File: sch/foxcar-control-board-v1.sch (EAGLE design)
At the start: 118 parts, among them J1 USB_MICROB, J2 MICROSD, J3 XBEE-PRO, U1 SPX29300, U2 HMC5883LSMD, U3 STM32F4V, U4 VNH5019, U6 MPU6000

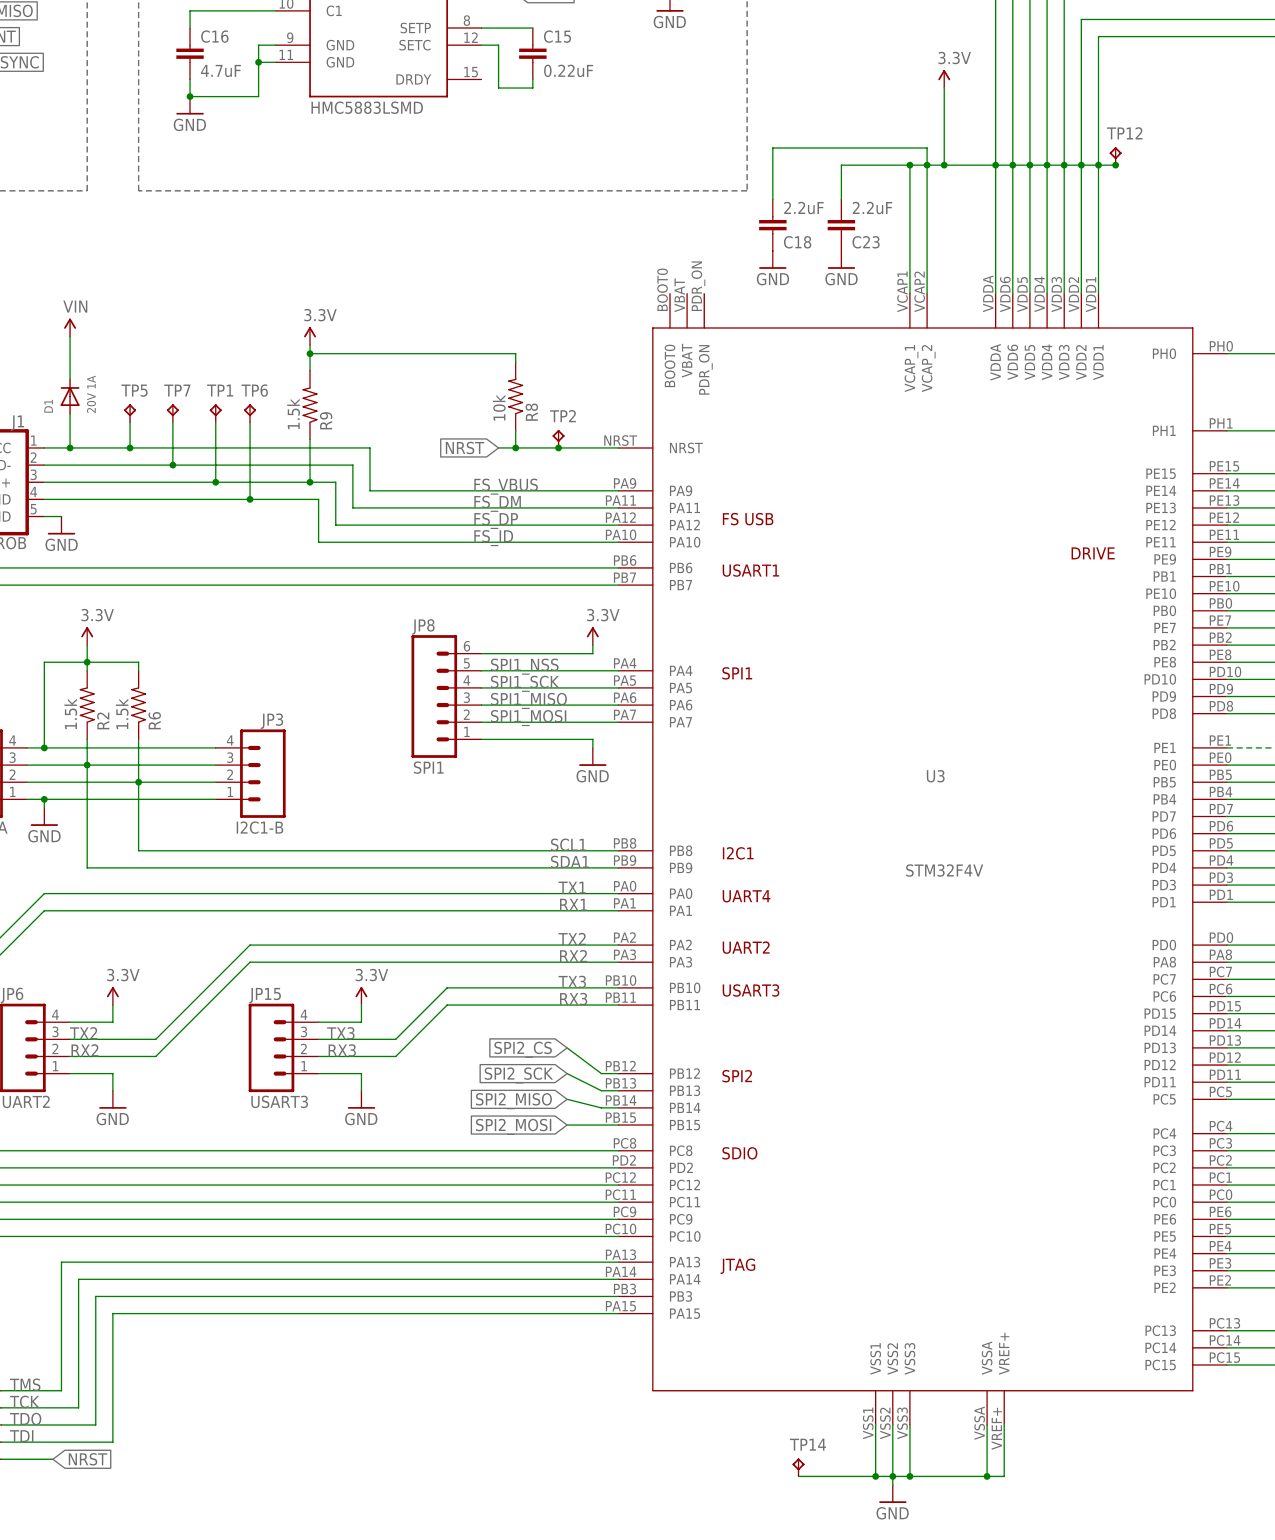
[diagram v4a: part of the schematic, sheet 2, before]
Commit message: Trying a new technique: placing all components around the stm32f4 with relatively direct paths, then seeing how badly I can fuck it up.
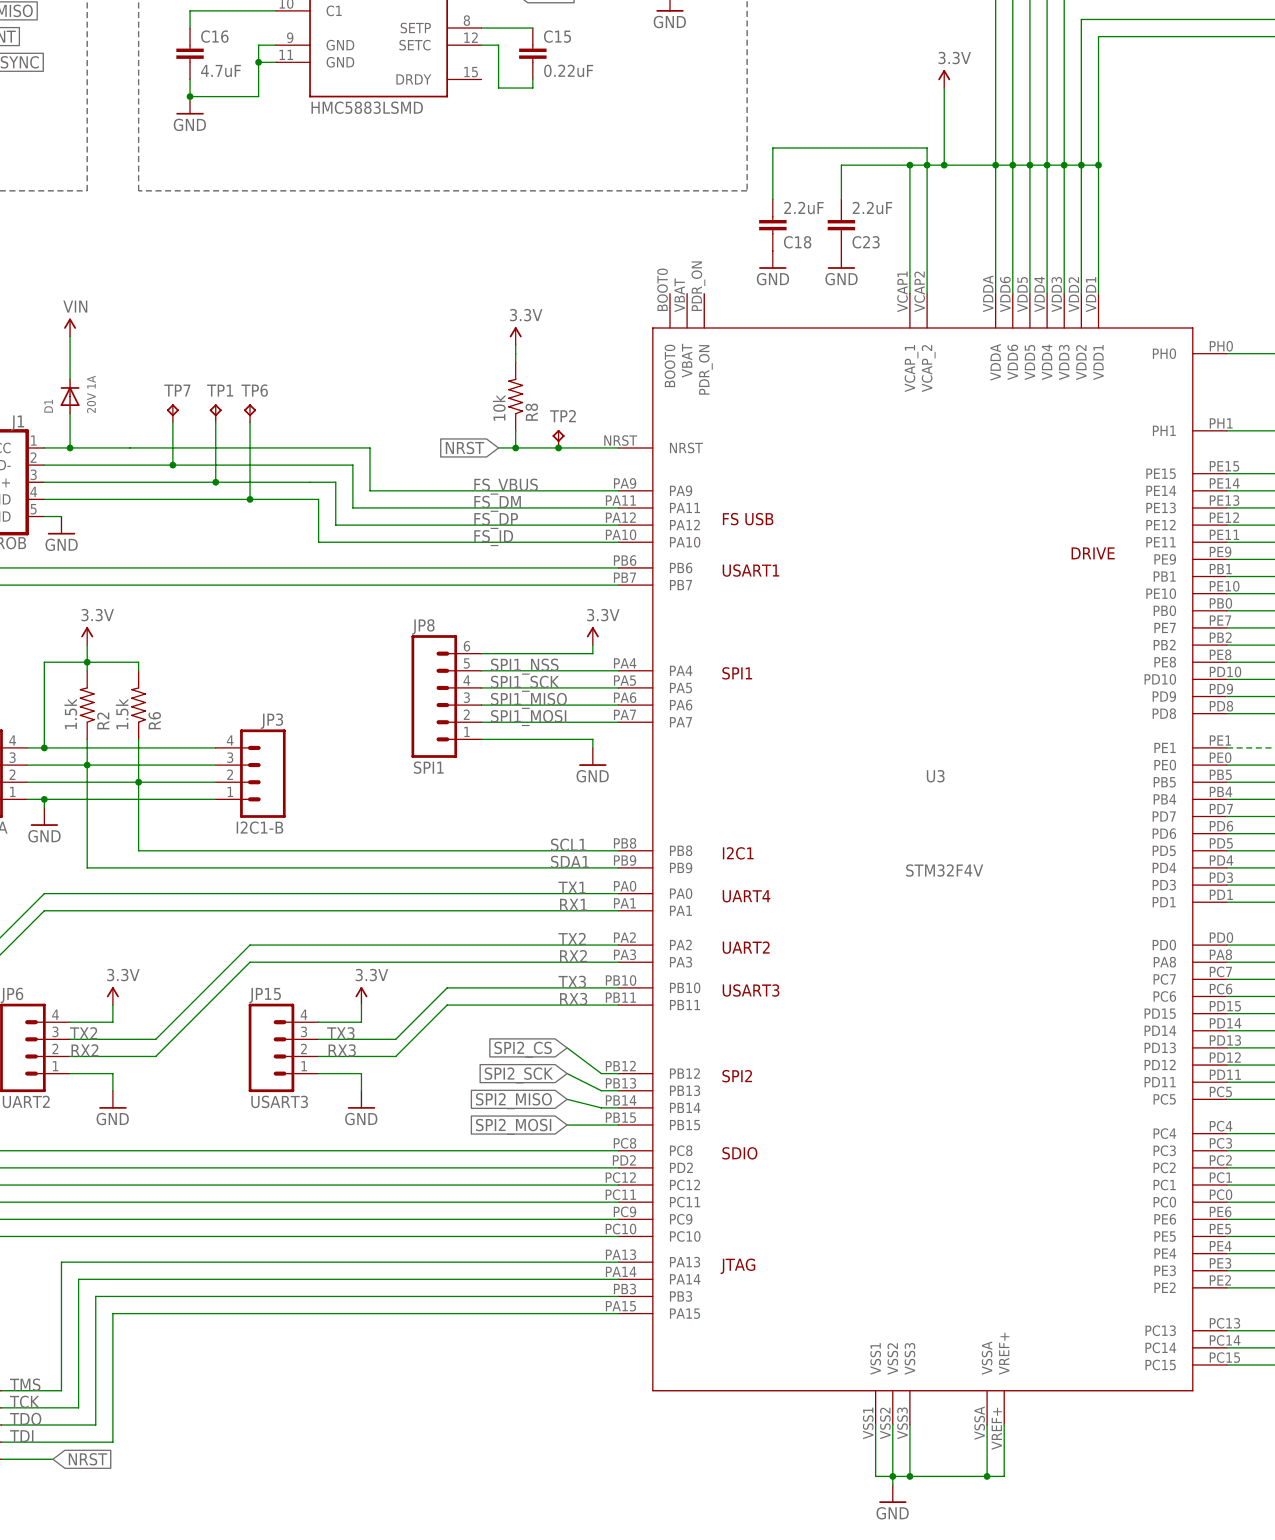
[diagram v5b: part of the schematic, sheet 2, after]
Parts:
- removed R9: 1.5k, SparkFun-Passives:RESISTOR0402-RES
- removed TP12, TP14, TP5: TPTP06R, testpad:TPTP06R
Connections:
- net 3.3V: no longer R9.2, TP12.TP
- net FS_DP: no longer R9.1
- net FS_VBUS: no longer TP5.TP
- net GND: no longer TP14.TP
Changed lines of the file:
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@@
 <part name="J1" library="SparkFun" deviceset="USB_MICROB_PLUG" device="-PTH" value="USB_MICROB"/>
 <part name="DIG_GND11" library="SparkFun-Aesthetics" deviceset="GND" device="" value="GND"/>
-<part name="R9" library="SparkFun-Passives" deviceset="RESISTOR" device="0402-RES" value="1.5k"/>
 <part name="TP1" library="testpad" deviceset="TP" device="TP06R"/>
-<part name="TP5" library="testpad" deviceset="TP" device="TP06R"/>
 <part name="TP7" library="testpad" deviceset="TP" device="TP06R"/>
 <part name="P+19" library="SparkFun-Aesthetics" deviceset="3.3V" device=""/>
@@
 <part name="DIG_GND26" library="SparkFun-Aesthetics" deviceset="GND" device="" value="GND"/>
 <part name="DIG_GND27" library="SparkFun-Aesthetics" deviceset="GND" device="" value="GND"/>
-<part name="TP12" library="testpad" deviceset="TP" device="TP06R"/>
 <part name="P+1" library="SparkFun-Aesthetics" deviceset="3.3V" device=""/>
 <part name="C21" library="SparkFun-Passives" deviceset="CAP" device="0402-CAP" value="100nF"/>
@@
 <part name="DIG_GND31" library="SparkFun-Aesthetics" deviceset="GND" device="" value="GND"/>
 <part name="DIG_GND32" library="SparkFun-Aesthetics" deviceset="GND" device="" value="GND"/>
-<part name="TP14" library="testpad" deviceset="TP" device="TP06R"/>
 <part name="C9" library="SparkFun-Passives" deviceset="CAP" device="0402-CAP" value="100nF"/>
 <part name="DIG_GND33" library="SparkFun-Aesthetics" deviceset="GND" device="" value="GND"/>
@@
 <instance part="J1" gate="G$1" x="106.68" y="165.1" rot="MR0"/>
 <instance part="DIG_GND11" gate="1" x="116.84" y="157.48" rot="MR0"/>
-<instance part="R9" gate="G$1" x="153.67" y="176.53" rot="MR90"/>
 <instance part="TP1" gate="G$1" x="139.7" y="176.53"/>
-<instance part="TP5" gate="G$1" x="127" y="176.53"/>
 <instance part="TP7" gate="G$1" x="133.35" y="176.53"/>
-<instance part="P+19" gate="G$1" x="153.67" y="185.42"/>
+<instance part="P+19" gate="G$1" x="184.15" y="185.42"/>
 <instance part="TP6" gate="G$1" x="144.78" y="176.53"/>
 <instance part="R8" gate="G$1" x="184.15" y="177.8" rot="MR90"/>
@@
 <instance part="DIG_GND26" gate="1" x="232.41" y="196.85" rot="MR0"/>
 <instance part="DIG_GND27" gate="1" x="222.25" y="196.85" rot="MR0"/>
-<instance part="TP12" gate="G$1" x="273.05" y="214.63"/>
 <instance part="P+1" gate="G$1" x="247.65" y="223.52"/>
 <instance part="C21" gate="G$1" x="356.87" y="215.9" rot="MR180"/>
@@
 <instance part="DIG_GND31" gate="1" x="330.2" y="171.45"/>
 <instance part="DIG_GND32" gate="1" x="240.03" y="13.97"/>
-<instance part="TP14" gate="G$1" x="226.06" y="20.32"/>
 <instance part="C9" gate="G$1" x="369.57" y="215.9" rot="MR180"/>
 <instance part="DIG_GND33" gate="1" x="369.57" y="205.74" rot="MR0"/>
@@
 </segment>
 <segment>
-<pinref part="R9" gate="G$1" pin="2"/>
 <pinref part="P+19" gate="G$1" pin="3.3V"/>
-<wire x1="153.67" y1="181.61" x2="153.67" y2="184.15" width="0.15" layer="91"/>
 <pinref part="R8" gate="G$1" pin="2"/>
-<wire x1="153.67" y1="184.15" x2="153.67" y2="185.42" width="0.15" layer="91"/>
 <wire x1="184.15" y1="182.88" x2="184.15" y2="184.15" width="0.15" layer="91"/>
-<wire x1="153.67" y1="184.15" x2="184.15" y2="184.15" width="0.15" layer="91"/>
-<junction x="153.67" y="184.15"/>
+<wire x1="184.15" y1="185.42" x2="184.15" y2="184.15" width="0.15" layer="91"/>
 </segment>
 <segment>
@@
 <wire x1="242.57" y1="193.04" x2="242.57" y2="212.09" width="0.15" layer="91"/>
 <pinref part="U3" gate="G$1" pin="VCAP_1"/>
-<pinref part="TP12" gate="G$1" pin="TP"/>
-<junction x="273.05" y="212.09"/>
-<wire x1="270.51" y1="212.09" x2="273.05" y2="212.09" width="0.15" layer="91"/>
 <pinref part="U3" gate="G$1" pin="VDDA"/>
 <wire x1="255.27" y1="193.04" x2="255.27" y2="212.09" width="0.15" layer="91"/>
@@
 <pinref part="DIG_GND32" gate="1" pin="GND"/>
 <junction x="240.03" y="17.78"/>
-<pinref part="TP14" gate="G$1" pin="TP"/>
 <wire x1="240.03" y1="17.78" x2="237.49" y2="17.78" width="0.15" layer="91"/>
-<wire x1="237.49" y1="17.78" x2="226.06" y2="17.78" width="0.15" layer="91"/>
 <wire x1="240.03" y1="17.78" x2="240.03" y2="25.4" width="0.15" layer="91"/>
 <wire x1="240.03" y1="17.78" x2="242.57" y2="17.78" width="0.15" layer="91"/>
@@
 <pinref part="U3" gate="G$1" pin="VSS2"/>
 <pinref part="U3" gate="G$1" pin="VSS3"/>
-<junction x="237.49" y="17.78"/>
 <wire x1="242.57" y1="17.78" x2="254" y2="17.78" width="0.15" layer="91"/>
 <pinref part="U3" gate="G$1" pin="VSSA"/>
@@
 <wire x1="157.48" y1="165.1" x2="157.48" y2="158.75" width="0.15" layer="91"/>
 <wire x1="157.48" y1="158.75" x2="199.39" y2="158.75" width="0.15" layer="91"/>
-<wire x1="153.67" y1="165.1" x2="153.67" y2="171.45" width="0.15" layer="91"/>
-<junction x="153.67" y="165.1"/>
-<pinref part="R9" gate="G$1" pin="1"/>
 <pinref part="J1" gate="G$1" pin="D+"/>
 <label x="177.8" y="158.75" size="1.778" layer="95"/>
@@
 <wire x1="118.11" y1="170.18" x2="118.11" y2="175.26" width="0.15" layer="91"/>
 <wire x1="118.11" y1="170.18" x2="127" y2="170.18" width="0.15" layer="91"/>
-<pinref part="TP5" gate="G$1" pin="TP"/>
 <wire x1="127" y1="170.18" x2="162.56" y2="170.18" width="0.15" layer="91"/>
 <wire x1="162.56" y1="170.18" x2="162.56" y2="163.83" width="0.15" layer="91"/>
 <wire x1="162.56" y1="163.83" x2="199.39" y2="163.83" width="0.15" layer="91"/>
-<wire x1="127" y1="173.99" x2="127" y2="170.18" width="0.15" layer="91"/>
-<junction x="127" y="170.18"/>
 <junction x="118.11" y="170.18"/>
 <label x="177.8" y="163.83" size="1.778" layer="95"/>

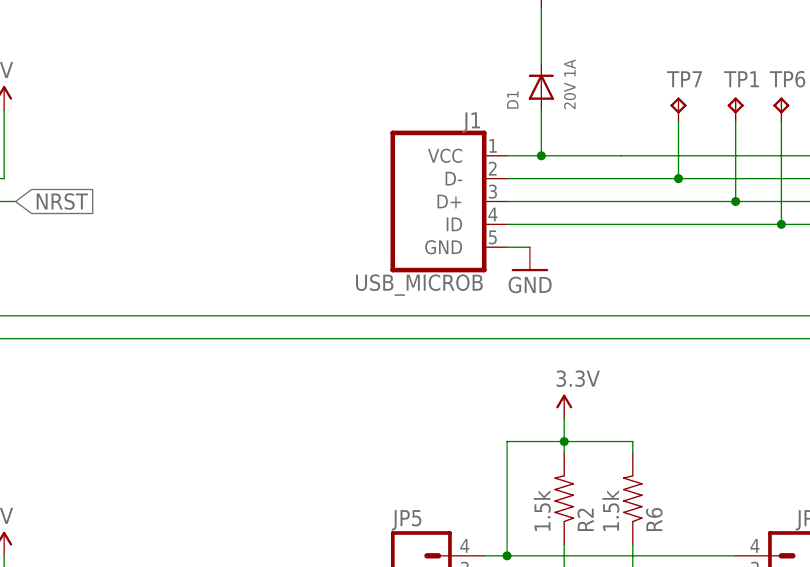
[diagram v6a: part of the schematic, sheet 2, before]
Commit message: Everything laid out except for the power stuff.
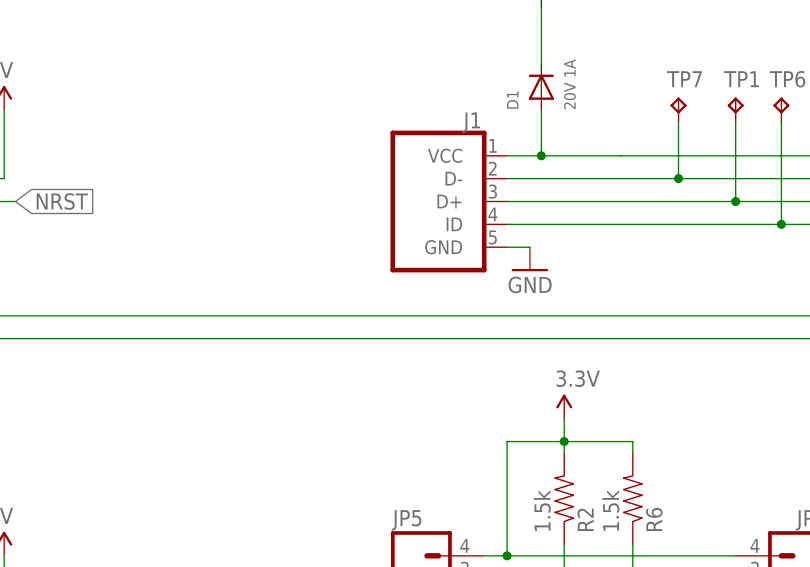
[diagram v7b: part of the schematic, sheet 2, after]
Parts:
- J1: value USB_MICROB -> USB_MICROB_PLUG-PTH
- JP16, JP17, JP18, JP19, JP20, JP21, JP22, JP23, JP24: value M01PTH_LONGPAD -> M01PTH; device SparkFun-Connectors:M01PTH_LONGPAD -> SparkFun-Connectors:M01PTH
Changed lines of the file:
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@@
 <part name="DIG_GND9" library="SparkFun-Aesthetics" deviceset="GND" device="" value="GND"/>
 <part name="P+18" library="SparkFun-Aesthetics" deviceset="3.3V" device=""/>
-<part name="J1" library="SparkFun" deviceset="USB_MICROB_PLUG" device="-PTH" value="USB_MICROB"/>
+<part name="J1" library="SparkFun" deviceset="USB_MICROB_PLUG" device="-PTH" value=""/>
 <part name="DIG_GND11" library="SparkFun-Aesthetics" deviceset="GND" device="" value="GND"/>
-<part name="TP1" library="testpad" deviceset="TP" device="TP06R"/>
-<part name="TP7" library="testpad" deviceset="TP" device="TP06R"/>
+<part name="TP1" library="testpad" deviceset="TP" device="TP06R" value=""/>
+<part name="TP7" library="testpad" deviceset="TP" device="TP06R" value=""/>
 <part name="P+19" library="SparkFun-Aesthetics" deviceset="3.3V" device=""/>
-<part name="TP6" library="testpad" deviceset="TP" device="TP06R"/>
+<part name="TP6" library="testpad" deviceset="TP" device="TP06R" value=""/>
 <part name="R8" library="SparkFun-Passives" deviceset="RESISTOR" device="0402-RES" value="10k"/>
 <part name="TP2" library="testpad" deviceset="TP" device="TP06R" value=""/>
@@
 <part name="JP1" library="SparkFun-Connectors" deviceset="M01" device="PTH_LONGPAD" value=""/>
 <part name="JP10" library="SparkFun-Connectors" deviceset="M01" device="PTH_LONGPAD" value=""/>
-<part name="JP16" library="SparkFun-Connectors" deviceset="M01" device="PTH_LONGPAD" value=""/>
-<part name="JP17" library="SparkFun-Connectors" deviceset="M01" device="PTH_LONGPAD" value=""/>
-<part name="JP18" library="SparkFun-Connectors" deviceset="M01" device="PTH_LONGPAD" value=""/>
-<part name="JP19" library="SparkFun-Connectors" deviceset="M01" device="PTH_LONGPAD" value=""/>
-<part name="JP20" library="SparkFun-Connectors" deviceset="M01" device="PTH_LONGPAD" value=""/>
-<part name="JP21" library="SparkFun-Connectors" deviceset="M01" device="PTH_LONGPAD" value=""/>
-<part name="JP22" library="SparkFun-Connectors" deviceset="M01" device="PTH_LONGPAD" value=""/>
-<part name="JP23" library="SparkFun-Connectors" deviceset="M01" device="PTH_LONGPAD" value=""/>
-<part name="JP24" library="SparkFun-Connectors" deviceset="M01" device="PTH_LONGPAD" value=""/>
+<part name="JP16" library="SparkFun-Connectors" deviceset="M01" device="PTH" value=""/>
+<part name="JP17" library="SparkFun-Connectors" deviceset="M01" device="PTH" value=""/>
+<part name="JP18" library="SparkFun-Connectors" deviceset="M01" device="PTH" value=""/>
+<part name="JP19" library="SparkFun-Connectors" deviceset="M01" device="PTH" value=""/>
+<part name="JP20" library="SparkFun-Connectors" deviceset="M01" device="PTH" value=""/>
+<part name="JP21" library="SparkFun-Connectors" deviceset="M01" device="PTH" value=""/>
+<part name="JP22" library="SparkFun-Connectors" deviceset="M01" device="PTH" value=""/>
+<part name="JP23" library="SparkFun-Connectors" deviceset="M01" device="PTH" value=""/>
+<part name="JP24" library="SparkFun-Connectors" deviceset="M01" device="PTH" value=""/>
 <part name="JP25" library="SparkFun-Connectors" deviceset="M01" device="PTH_LONGPAD" value=""/>
 <part name="JP26" library="SparkFun-Connectors" deviceset="M01" device="PTH_LONGPAD" value=""/>
